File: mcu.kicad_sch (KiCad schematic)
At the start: 34 parts, among them J2 SWD, J3 SWC, U1 NRF52840-QIAA-R, Y1 32.768 kHz, Y2 32 MHz

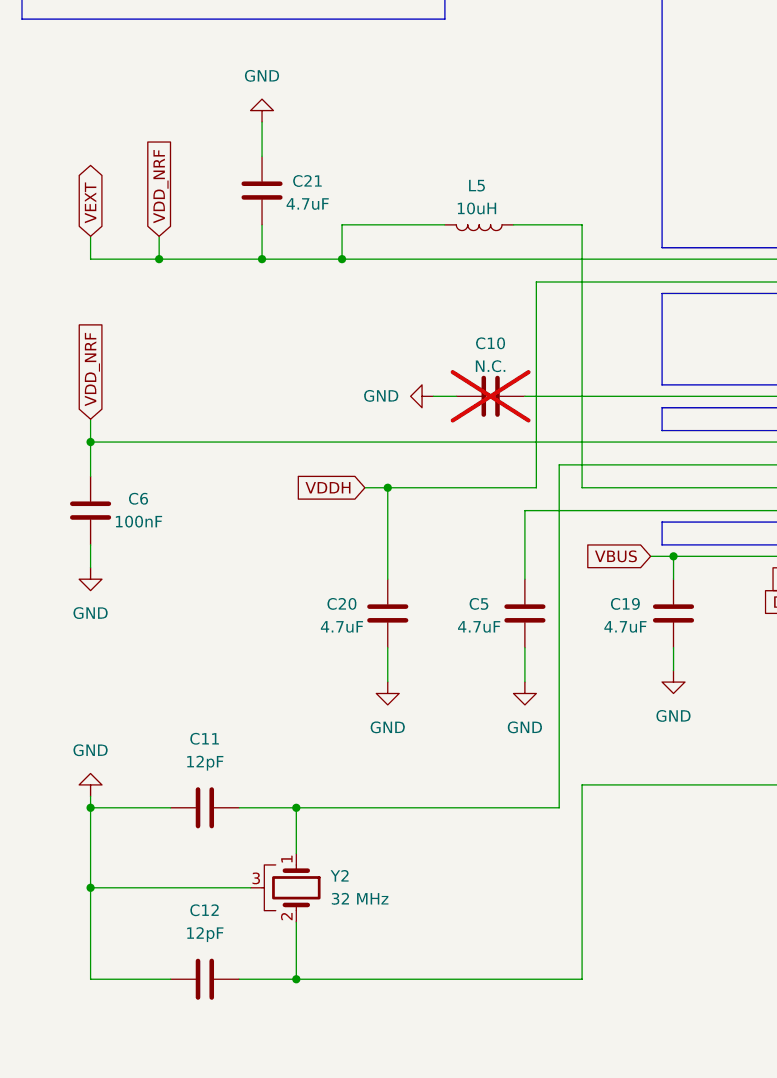
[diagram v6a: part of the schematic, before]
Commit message: Updated Footprints
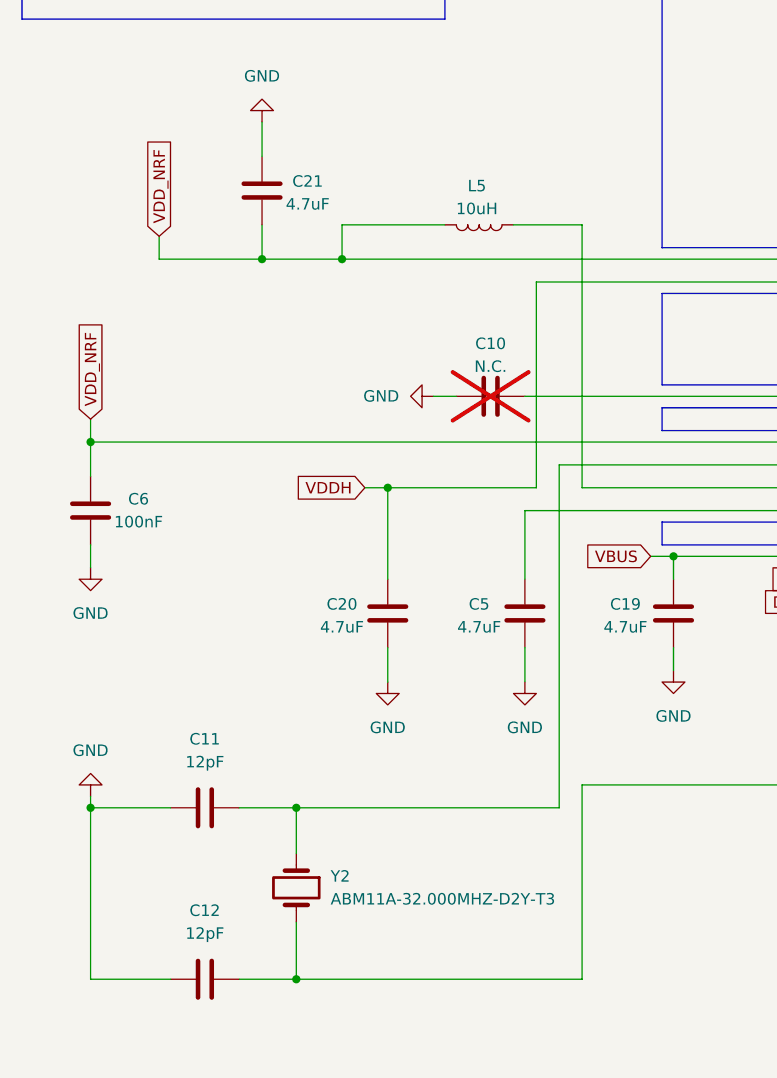
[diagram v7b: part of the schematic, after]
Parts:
- J2, J3: footprint TestPoint:TestPoint_Pad_2.5x2.5mm -> TestPoint:TestPoint_Pad_D1.5mm
- R1: footprint (none) -> Resistor_SMD:R_0402_1005Metric_Pad0.72x0.64mm_HandSolder
- R9: footprint (none) -> Resistor_SMD:R_0603_1608Metric
- Y2: value 32 MHz -> ABM11A-32.000MHZ-D2Y-T3; footprint (none) -> Crystal:Crystal_SMD_2016-4Pin_2.0x1.6mm; symbol Device:Crystal_GND3 -> Device:Crystal
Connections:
- net GND: no longer Y2.3
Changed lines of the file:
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@@
 	)
 	(junction
-		(at 38.1 172.72)
-		(diameter 0)
-		(color 0 0 0 0)
-	)
-	(junction
 		(at 60.96 163.83)
 		(diameter 0)
@@
 	)
 	(junction
-		(at 45.72 102.87)
-		(diameter 0)
-		(color 0 0 0 0)
-	)
-	(junction
 		(at 194.31 49.53)
 		(diameter 0)
@@
 	(wire
 		(pts
-			(xy 38.1 182.88) (xy 38.1 172.72)
+			(xy 38.1 163.83) (xy 38.1 182.88)
 		)
 		(stroke
@@
 		)
 	)
-	(wire
-		(pts
-			(xy 38.1 100.33) (xy 38.1 102.87)
-		)
-		(stroke
-			(width 0)
-			(type default)
-		)
-	)
 	(polyline
 		(pts
@@
 	(wire
 		(pts
-			(xy 38.1 102.87) (xy 45.72 102.87)
-		)
-		(stroke
-			(width 0)
-			(type default)
-		)
-	)
-	(wire
-		(pts
 			(xy 209.55 125.73) (xy 209.55 26.67)
 		)
@@
 	(wire
 		(pts
-			(xy 38.1 172.72) (xy 55.88 172.72)
-		)
-		(stroke
-			(width 0)
-			(type default)
-		)
-	)
-	(wire
-		(pts
 			(xy 118.11 123.19) (xy 38.1 123.19)
 		)
@@
 	(wire
 		(pts
-			(xy 38.1 172.72) (xy 38.1 163.83)
-		)
-		(stroke
-			(width 0)
-			(type default)
-		)
-	)
-	(wire
-		(pts
 			(xy 46.99 182.88) (xy 38.1 182.88)
 		)
@@
 		)
 	)
-	(global_label "VEXT"
-		(shape bidirectional)
-		(at 38.1 100.33 90)
-		(fields_autoplaced yes)
-		(effects
-			(font
-				(size 1.27 1.27)
-			)
-			(justify left)
-		)
-		(property "Intersheetrefs" "${INTERSHEET_REFS}"
-			(at 38.1 91.8188 90)
-			(effects
-				(font
-					(size 1.27 1.27)
-				)
-				(justify left)
-				(hide yes)
-			)
-		)
-	)
 	(global_label "D-"
 		(shape input)
@@
 			)
 		)
-		(property "Footprint" "TestPoint:TestPoint_Pad_2.5x2.5mm"
+		(property "Footprint" "TestPoint:TestPoint_Pad_D1.5mm"
 			(at 138.43 182.88 0)
 			(effects
@@
 			)
 		)
-		(property "Footprint" ""
+		(property "Footprint" "Resistor_SMD:R_0402_1005Metric_Pad0.72x0.64mm_HandSolder"
 			(at 264.16 122.428 90)
 			(effects
@@
 			)
 		)
-		(property "Footprint" ""
+		(property "Footprint" "Resistor_SMD:R_0603_1608Metric"
 			(at 144.78 174.498 90)
 			(effects
@@
 			)
 		)
-		(property "Footprint" "TestPoint:TestPoint_Pad_2.5x2.5mm"
+		(property "Footprint" "TestPoint:TestPoint_Pad_D1.5mm"
 			(at 138.43 189.23 0)
 			(effects
@@
 	)
 	(symbol
-		(lib_id "Device:Crystal_GND3")
+		(lib_id "Device:Crystal")
 		(at 60.96 172.72 270)
 		(unit 1)
@@
 			)
 		)
-		(property "Value" "32 MHz"
+		(property "Value" "ABM11A-32.000MHZ-D2Y-T3"
 			(at 64.77 173.9899 90)
 			(effects
@@
 			)
 		)
-		(property "Footprint" ""
+		(property "Footprint" "Crystal:Crystal_SMD_2016-4Pin_2.0x1.6mm"
 			(at 60.96 172.72 0)
 			(effects
@@
 			)
 		)
-		(property "Description" "Three pin crystal, GND on pin 3, XTAL SMD 2016, 32 MHz, Cl=8 pF, Total Tol: ±40 ppm"
+		(property "Description" "Two pin crystal"
 			(at 60.96 172.72 0)
 			(effects
@@
 		(pin "1"
 		)
-		(pin "3"
-		)
 		(instances

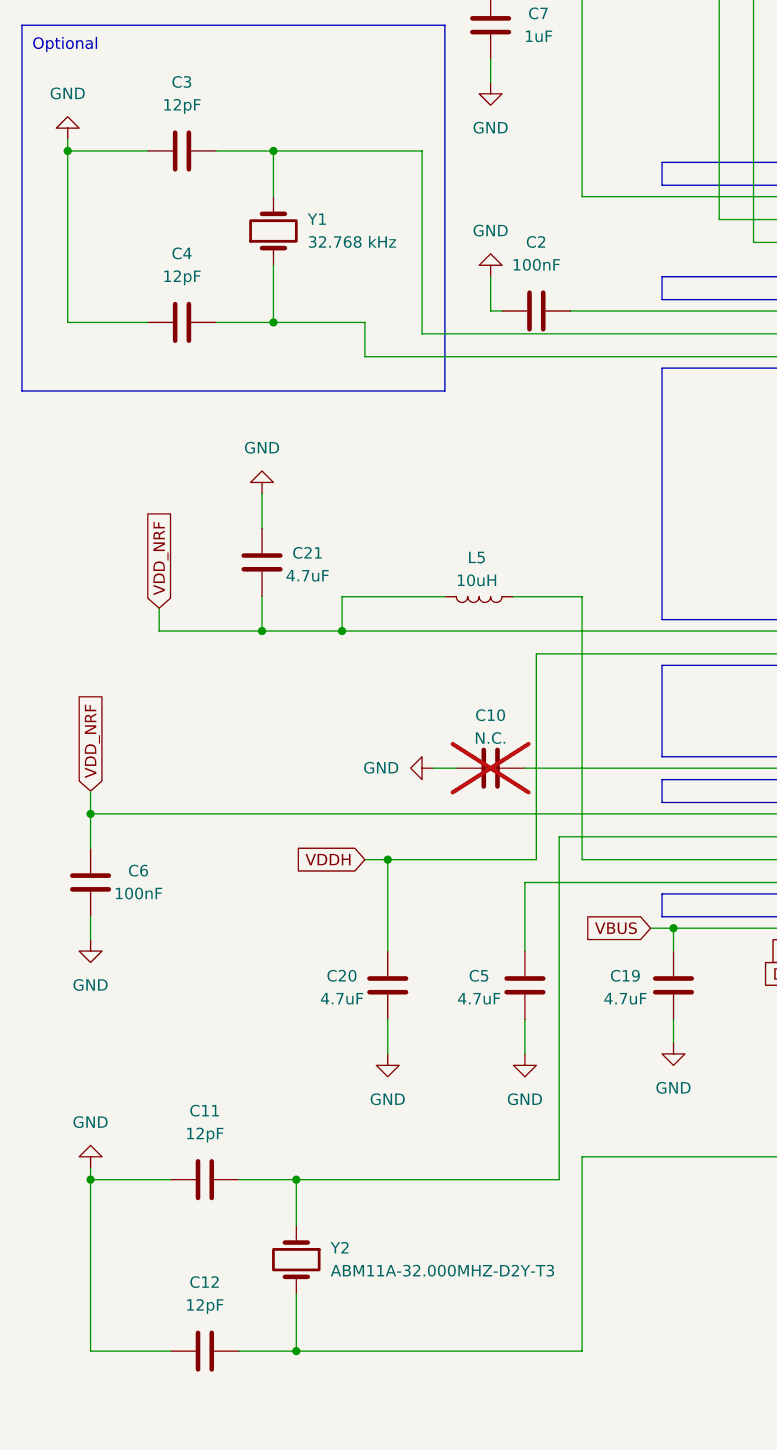
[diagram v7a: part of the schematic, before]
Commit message: Updated Footprints
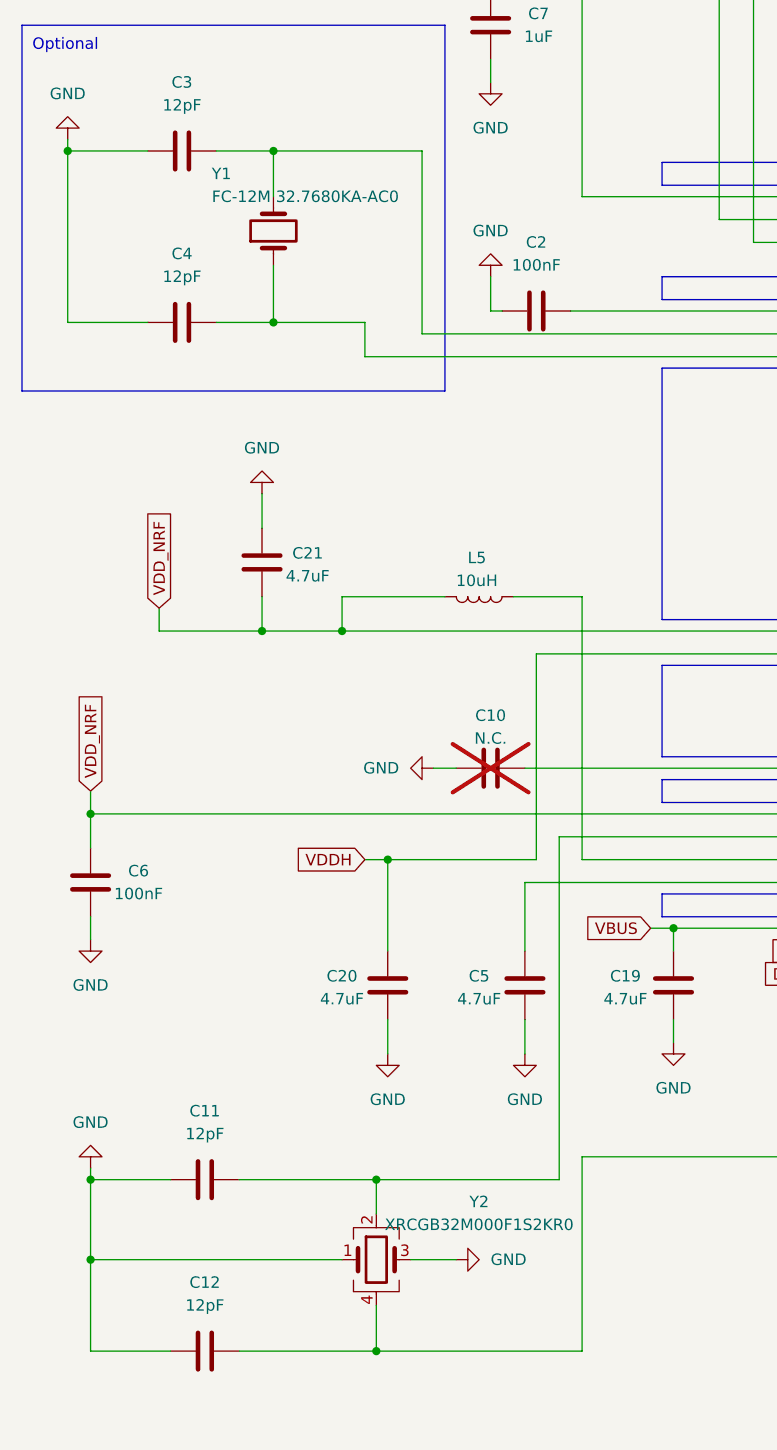
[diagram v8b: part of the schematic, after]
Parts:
- removed Y2: ABM11A-32.000MHZ-D2Y-T3, Crystal:Crystal_SMD_2016-4Pin_2.0x1.6mm, symbol Device:Crystal
- added Y2: XRCGB32M000F1S2KR0, Crystal:Crystal_SMD_2016-4Pin_2.0x1.6mm, symbol Device:Crystal_GND24
- Y1: value 32.768 kHz -> FC-12M 32.7680KA-AC0
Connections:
- net GND: now also Y2.1, Y2.3
- net at C12.1, U1.B24 (XC1): now also Y2.4
- net at C11.1, U1.A23 (XC2): now also Y2.2
